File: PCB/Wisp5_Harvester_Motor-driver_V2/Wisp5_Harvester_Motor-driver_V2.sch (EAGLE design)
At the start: 29 parts, among them M1 PINHEAD_PINHD-1X2-1.27MM, M2 PINHEAD_PINHD-1X2-1.27MM, U1 BQ25570

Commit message: Fix the naming on the pcb and of the parts!
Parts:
- L1: value 22uH -> (none)
- L2: value 10uH -> (none)
- renumbered U$1 to WISP, U$2 to U2, U$3 to U3

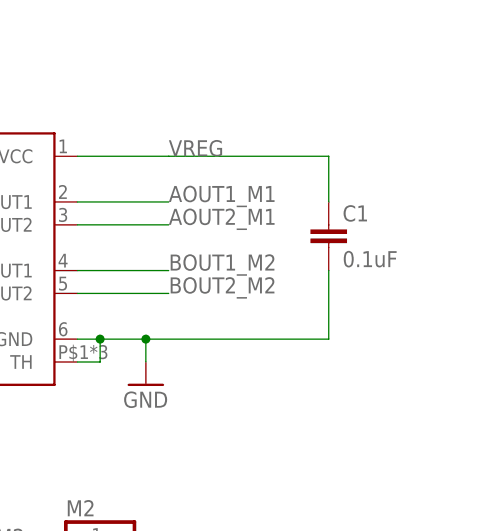
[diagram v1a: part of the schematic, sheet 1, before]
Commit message: Add a exta bulk capacitor near the hbridge!
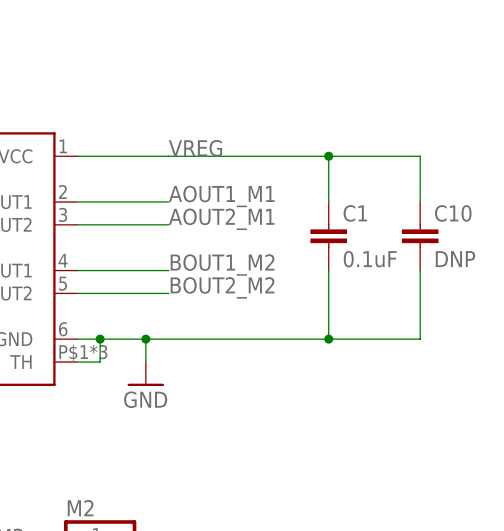
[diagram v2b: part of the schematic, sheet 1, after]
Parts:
- added C10: DNP, rcl:C-EUC0805
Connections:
- net GND: now also C10.2
- net VREG: now also C10.1
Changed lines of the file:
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@@
 <part name="GND15" library="Wisp5_Harvester_Motor-driver_V2" deviceset="GND" device=""/>
 <part name="MAX44000" library="Wisp5_Harvester_Motor-driver_V2" deviceset="PINHEAD_PINHD-1X4-1.27MM" device=""/>
+<part name="C10" library="rcl" library_urn="urn:adsk.eagle:library:334" deviceset="C-EU" device="C0805" value="DNP"/>
 </parts>
 <sheets>
@@
 <instance part="GND15" gate="1" x="66.04" y="22.86"/>
 <instance part="MAX44000" gate="G$1" x="83.82" y="15.24"/>
+<instance part="C10" gate="G$1" x="215.9" y="71.12"/>
 </instances>
 <busses>
@@
 <junction x="185.42" y="58.42"/>
 <junction x="180.34" y="58.42"/>
+<pinref part="C10" gate="G$1" pin="2"/>
+<wire x1="205.74" y1="58.42" x2="215.9" y2="58.42" width="0.1524" layer="91"/>
+<wire x1="215.9" y1="58.42" x2="215.9" y2="66.04" width="0.1524" layer="91"/>
+<junction x="205.74" y="58.42"/>
 </segment>
 <segment>
@@
 <wire x1="205.74" y1="78.74" x2="205.74" y2="73.66" width="0.127" layer="91"/>
 <label x="187.96" y="78.74" size="1.778" layer="95"/>
-</segment>
-<segment>
+<pinref part="C10" gate="G$1" pin="1"/>
+<wire x1="205.74" y1="78.74" x2="215.9" y2="78.74" width="0.1524" layer="91"/>
+<wire x1="215.9" y1="78.74" x2="215.9" y2="73.66" width="0.1524" layer="91"/>
+<junction x="205.74" y="78.74"/>
+</segment>
+<segment>

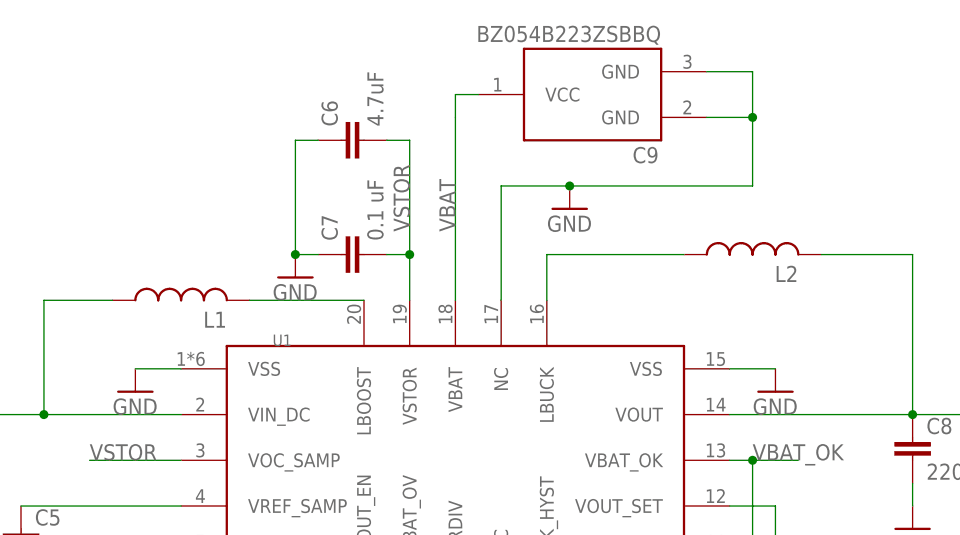
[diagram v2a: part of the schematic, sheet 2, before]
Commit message: Small changes to the layout and added missing inductor values!
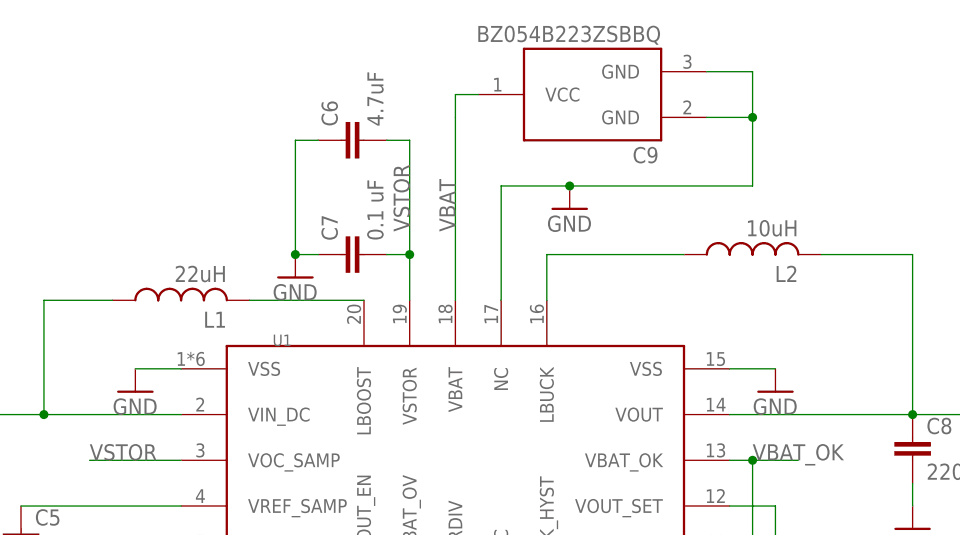
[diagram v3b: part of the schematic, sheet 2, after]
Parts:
- L1: value (none) -> 22uH
- L2: value (none) -> 10uH
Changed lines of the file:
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@@
 <part name="R2" library="resistor" library_urn="urn:adsk.eagle:library:348" deviceset="R-EU_" device="R0805" value="5.36M"/>
 <part name="R1" library="resistor" library_urn="urn:adsk.eagle:library:348" deviceset="R-EU_" device="R0805" value="7.50M"/>
-<part name="L1" library="Wisp5_Harvester_Motor-driver_V2" deviceset="COILCRAFT-LPS4018" device=""/>
-<part name="L2" library="Wisp5_Harvester_Motor-driver_V2" deviceset="COILCRAFT-LPS4018" device=""/>
+<part name="L1" library="Wisp5_Harvester_Motor-driver_V2" deviceset="COILCRAFT-LPS4018" device="" value="22uH"/>
+<part name="L2" library="Wisp5_Harvester_Motor-driver_V2" deviceset="COILCRAFT-LPS4018" device="" value="10uH"/>
 <part name="C8" library="Wisp5_Harvester_Motor-driver_V2" deviceset="C-EU" device="C1210" value="220uF"/>
 <part name="R6" library="resistor" library_urn="urn:adsk.eagle:library:348" deviceset="R-EU_" device="R0805" value="6.04M"/>
